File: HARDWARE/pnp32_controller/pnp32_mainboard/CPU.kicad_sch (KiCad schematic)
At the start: 1 part, among them U1 ESP32-PICO-V3

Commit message: update
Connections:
- net SPI_CS_B: now reaches U1.14 (GPIO25/ADC2_CH8/DAC_1)
- net SPI_CS_C: now reaches U1.15 (GPIO26/ADC2_CH9/DAC_2)
- net SPI_MISO: now reaches U1.22 (GPIO2/ADC2_CH2)
- net SPI_MOSI: now reaches U1.24 (GPIO4/ADC2_CH0)
- net SPI_CS_Y: now reaches U1.27 (GPIO20)
- net I2C_SDA: now reaches U1.31 (SD_CLK/GPIO6)
- net I2C_SCL: now reaches U1.32 (SD_DATA_0/GPIO7)
- net SPI_CLK: now reaches U1.34 (GPIO5)
- net SPI_CS_X: now reaches U1.38 (GPIO19)
- net SPI_CS_A: now reaches U1.39 (GPIO22)
- net SPI_CS_Z: now reaches U1.42 (GPIO21)
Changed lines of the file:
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@@
 	(generator_version "9.0")
 	(paper "A4")
+	(wire
+		(pts
+			(xy 161.29 49.53) (xy 134.62 49.53)
+		)
+		(stroke
+			(width 0)
+			(type default)
+		)
+	)
+	(wire
+		(pts
+			(xy 161.29 69.85) (xy 134.62 69.85)
+		)
+		(stroke
+			(width 0)
+			(type default)
+		)
+	)
+	(wire
+		(pts
+			(xy 161.29 57.15) (xy 134.62 57.15)
+		)
+		(stroke
+			(width 0)
+			(type default)
+		)
+	)
+	(wire
+		(pts
+			(xy 161.29 64.77) (xy 134.62 64.77)
+		)
+		(stroke
+			(width 0)
+			(type default)
+		)
+	)
+	(wire
+		(pts
+			(xy 161.29 80.01) (xy 134.62 80.01)
+		)
+		(stroke
+			(width 0)
+			(type default)
+		)
+	)
+	(wire
+		(pts
+			(xy 161.29 52.07) (xy 134.62 52.07)
+		)
+		(stroke
+			(width 0)
+			(type default)
+		)
+	)
+	(wire
+		(pts
+			(xy 161.29 54.61) (xy 134.62 54.61)
+		)
+		(stroke
+			(width 0)
+			(type default)
+		)
+	)
+	(wire
+		(pts
+			(xy 161.29 67.31) (xy 134.62 67.31)
+		)
+		(stroke
+			(width 0)
+			(type default)
+		)
+	)
+	(wire
+		(pts
+			(xy 161.29 77.47) (xy 134.62 77.47)
+		)
+		(stroke
+			(width 0)
+			(type default)
+		)
+	)
+	(wire
+		(pts
+			(xy 161.29 62.23) (xy 134.62 62.23)
+		)
+		(stroke
+			(width 0)
+			(type default)
+		)
+	)
+	(wire
+		(pts
+			(xy 161.29 59.69) (xy 134.62 59.69)
+		)
+		(stroke
+			(width 0)
+			(type default)
+		)
+	)
+	(hierarchical_label "SPI_MOSI"
+		(shape input)
+		(at 161.29 52.07 0)
+		(effects
+			(font
+				(size 1.27 1.27)
+			)
+			(justify left)
+		)
+	)
+	(hierarchical_label "SPI_CLK"
+		(shape input)
+		(at 161.29 54.61 0)
+		(effects
+			(font
+				(size 1.27 1.27)
+			)
+			(justify left)
+		)
+	)
+	(hierarchical_label "SPI_CS_Z"
+		(shape input)
+		(at 161.29 62.23 0)
+		(effects
+			(font
+				(size 1.27 1.27)
+			)
+			(justify left)
+		)
+	)
+	(hierarchical_label "SPI_MISO"
+		(shape input)
+		(at 161.29 49.53 0)
+		(effects
+			(font
+				(size 1.27 1.27)
+			)
+			(justify left)
+		)
+	)
+	(hierarchical_label "SPI_CS_C"
+		(shape input)
+		(at 161.29 69.85 0)
+		(effects
+			(font
+				(size 1.27 1.27)
+			)
+			(justify left)
+		)
+	)
+	(hierarchical_label "I2C_SCL"
+		(shape input)
+		(at 161.29 80.01 0)
+		(effects
+			(font
+				(size 1.27 1.27)
+			)
+			(justify left)
+		)
+	)
+	(hierarchical_label "SPI_CS_A"
+		(shape input)
+		(at 161.29 64.77 0)
+		(effects
+			(font
+				(size 1.27 1.27)
+			)
+			(justify left)
+		)
+	)
+	(hierarchical_label "SPI_CS_X"
+		(shape input)
+		(at 161.29 57.15 0)
+		(effects
+			(font
+				(size 1.27 1.27)
+			)
+			(justify left)
+		)
+	)
+	(hierarchical_label "SPI_CS_Y"
+		(shape input)
+		(at 161.29 59.69 0)
+		(effects
+			(font
+				(size 1.27 1.27)
+			)
+			(justify left)
+		)
+	)
+	(hierarchical_label "SPI_CS_B"
+		(shape input)
+		(at 161.29 67.31 0)
+		(effects
+			(font
+				(size 1.27 1.27)
+			)
+			(justify left)
+		)
+	)
+	(hierarchical_label "I2C_SDA"
+		(shape input)
+		(at 161.29 77.47 0)
+		(effects
+			(font
+				(size 1.27 1.27)
+			)
+			(justify left)
+		)
+	)
 	(symbol
 		(lib_id "fab_ESP:ESP32-PICO-V3")

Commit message: update
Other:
- company: (none) -> telelmetry.digital s.r.o.
- title: (none) -> pnp32 Motion Controller
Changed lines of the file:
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@@
 	(generator_version "9.0")
 	(paper "A4")
+	(title_block
+		(title "pnp32 Motion Controller")
+		(date "2025-08-01")
+		(rev "V0.1")
+		(company "telelmetry.digital s.r.o.")
+	)
 	(wire
 		(pts

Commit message: update
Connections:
- net +3.3V: now reaches U1.1 (VDDA), U1.43 (VDDA), U1.46 (VDDA)
- net +3.3V: now also U1.19 (VDD3P3_RTC), U1.26 (VDD_SDIO), U1.3 (VDD3P3), U1.37 (VDD3P3_CPU), U1.4 (VDD3P3)
- net VAC1: now reaches U1.10 (VDET_1/GPIO34/ADC1_CH6)
- net VAC2: now reaches U1.11 (VDET_2/GPIO35/ADC1_CH7)
- net ENABLE: now reaches U1.12 (32K_XP/GPIO32/ADC1_CH4)
- net E-STOP: now reaches U1.13 (32K_XN/GPIO33/ADC1_CH5)
- net PIN_RD: now reaches U1.17 (MTMS/GPIO14/ADC2_CH6)
- net RS485_A: now reaches U1.18 (MTDI/GPIO12/ADC2_CH5)
- net RS485_B: now reaches U1.20 (MTCK/GPIO13/ADC2_CH4)
- net PIN_WR: now reaches U1.21 (MTDO/GPIO15/ADC2_CH3)
- net WLED: now reaches U1.33 (SD_DATA_1/GPIO8)
- net GND: now reaches U1.49 (GND)
- net VAC_PUMP: now reaches U1.5 (SENSOR_VP/GPIO36/ADC1_CH0)
- net AIR1: now reaches U1.6 (SENSOR_CAPP/GPIO37/ADC1_CH1)
- net AIR2: now reaches U1.7 (SENSOR_CAPN/GPIO38/ADC1_CH2)
- net AIR_PUMP: now reaches U1.8 (SENSOR_VN/GPIO39/ADC1_CH3)

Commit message: update
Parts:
- added BZ1: Buzzer, Buzzer_Beeper:MagneticBuzzer_CUI_CMT-8504-100-SMT, symbol Device:Buzzer
- added C19, C20: 100n, Capacitor_SMD:C_0805_2012Metric, symbol Device:C_Small
- added D15, D16: SM4007, Diode_SMD:D_SOD-123F, symbol Device:D_Small
- added J16: FAN, Connector_JST:JST_PH_B2B-PH-SM4-TB_1x02-1MP_P2.00mm_Vertical, symbol Connector_Generic_MountingPin:Conn_01x02_MountingPin
- added Q7: AO3400A, Package_TO_SOT_SMD:SOT-23, symbol Transistor_FET:AO3400A
- added R14, R15: 4.7kΩ, fab_R:R_0402, symbol fab_R:R_4.7kΩ_0402
- added R53: 1k, Resistor_SMD:R_0805_2012Metric, symbol Device:R_Small
- added U5, U7: XGZP6857D, Package_DIP:DIP-6_W10.16mm, symbol index:XGZP6857D
- renumbered U1 to U6
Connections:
- net +3.3V: now also C19.1, C20.1, R14.1, R15.1, U5.2 (VDD), U7.2 (VDD)
- net GND: now also C19.2, C20.2, D16.2 (A), J16.2 (Pin_2), J16.MP (MountPin), Q7.2 (S), U5.6 (GND), U7.6 (GND)
- net I2C_SCL: now also R15.2, U5.5 (SCL), U7.5 (SCL)
- net I2C_SDA: now also R14.2, U5.4 (SDA), U7.4 (SDA)
- net X_STOP: now reaches U6.16 (GPIO27/ADC2_CH7)
- net LIGHT_BOTTOM: now reaches U6.28 (SD_DATA_2/GPIO9)
- net Y_STOP: now reaches U6.29 (SD_DATA_3/GPIO10)
- net Z_STOP: now reaches U6.30 (SD_CMD/GPIO11)
- net PIN_RD renamed PIN_RD/WR
- net PIN_WR renamed BUZZER
- net BUZZER: now also R53.1
- net WLED renamed LIGHT_TOP
- new net: BZ1.2 (+), D15.2 (A), Q7.3 (D)
- new net: Q7.1 (G), R53.2
- new net +5V: BZ1.1 (-), D15.1 (K), D16.1 (K), J16.1 (Pin_1)
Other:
- note added: "Ventilátor napájať priamo z 5V"

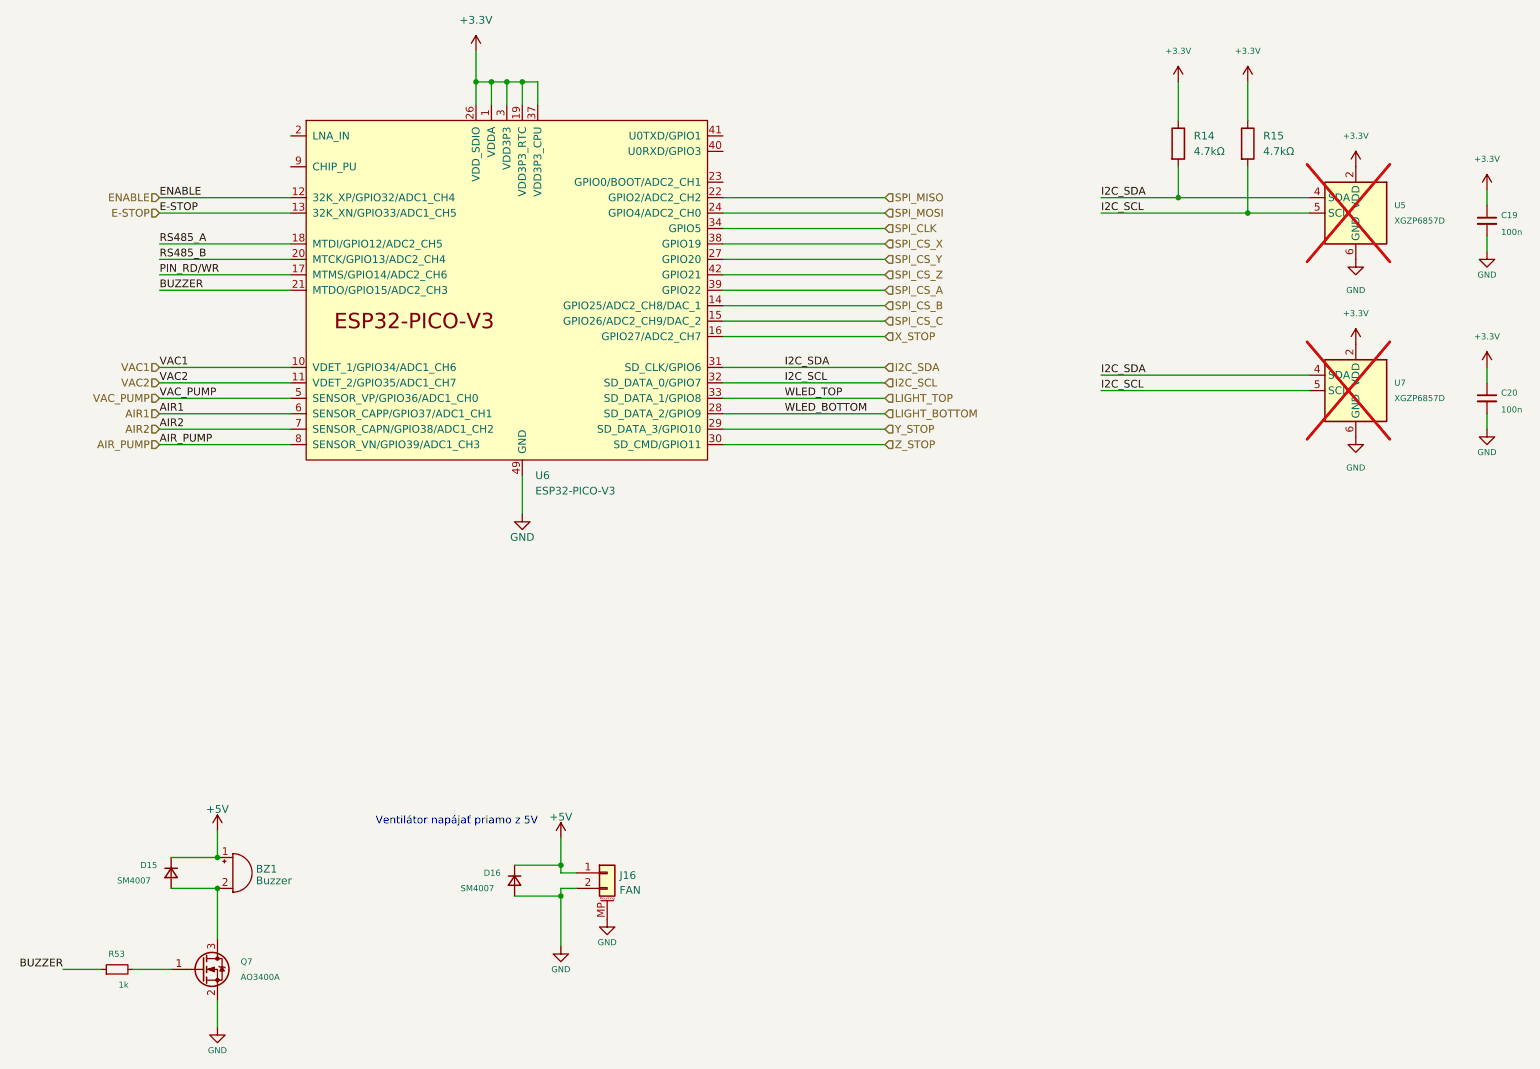
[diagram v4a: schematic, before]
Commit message: update_PSU
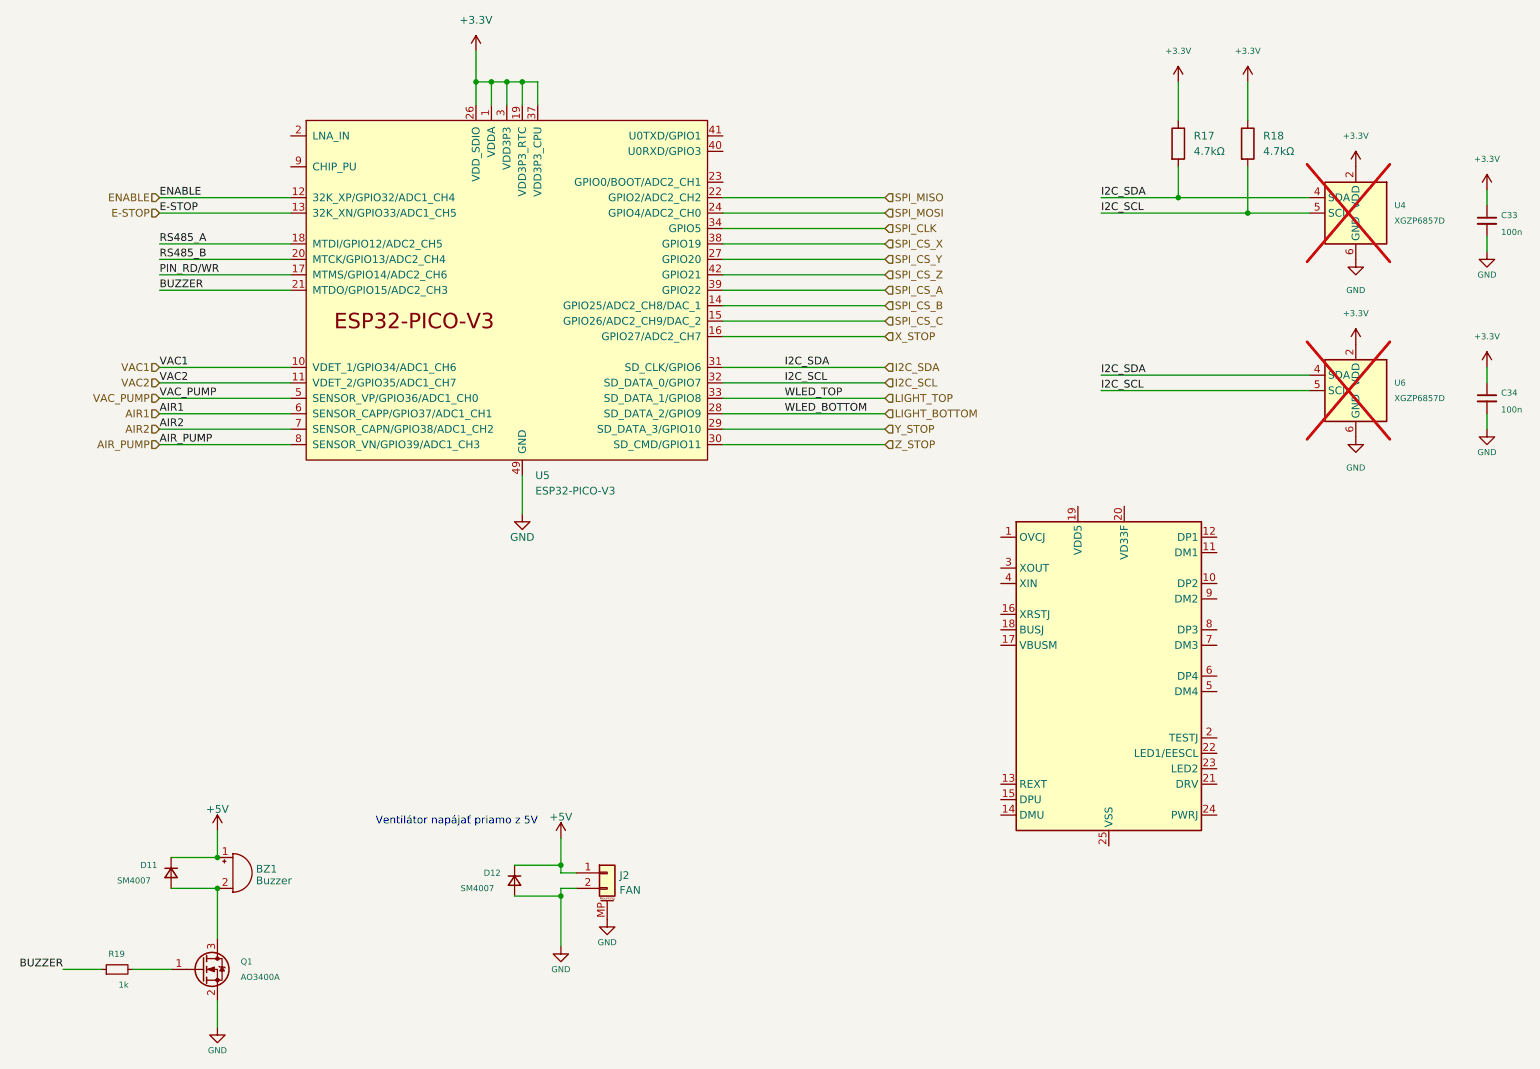
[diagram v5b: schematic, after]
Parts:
- added U7: FE1.1S-BQFN24B, fab_U:WQFN-24-1EP_4x4mm_P0.5mm_EP2.7x2.7mm, symbol fab_U:FE1.1S-BQFN24B
- renumbered C19 to C33, C20 to C34, D15 to D11, D16 to D12, J16 to J2, Q7 to Q1, R14 to R17, R15 to R18, R53 to R19, U5 to U4, U6 to U5, U7 to U6
